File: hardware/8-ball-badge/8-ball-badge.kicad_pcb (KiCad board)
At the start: 2 copper layers, 84 x 84 mm, 88 parts, among them J1 BattConn, J2 SAO Header 1, J3 SAO Header 2, Q1 AO3401A, Q2 S8050, SW1 SW_Push, SW2 TS-1187A-B-A-B, U1 TC4056A, U10 ME6210A33PG, U2 W25Q128JVSIQTR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

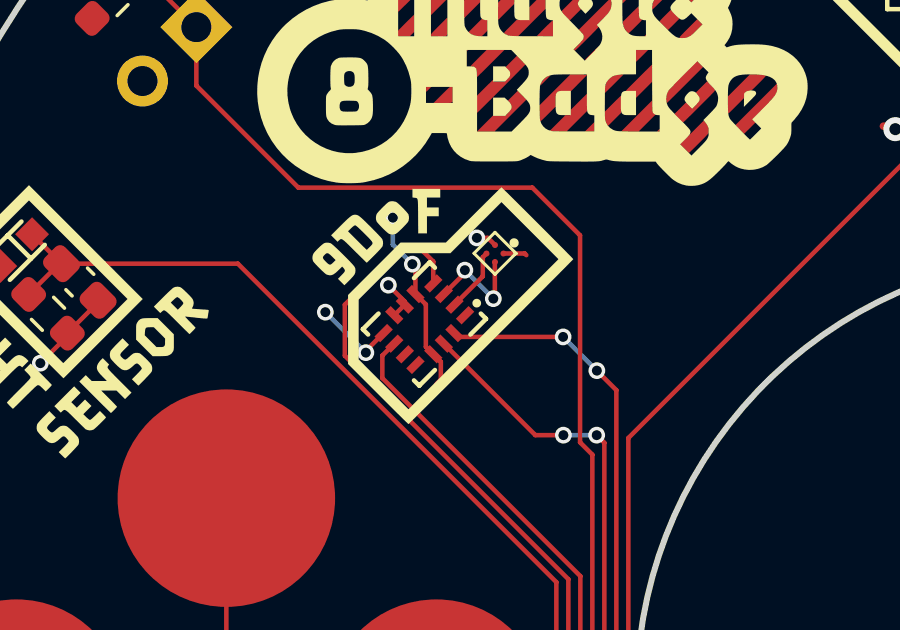
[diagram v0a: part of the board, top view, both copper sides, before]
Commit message: Fix issues with 9DoF chip
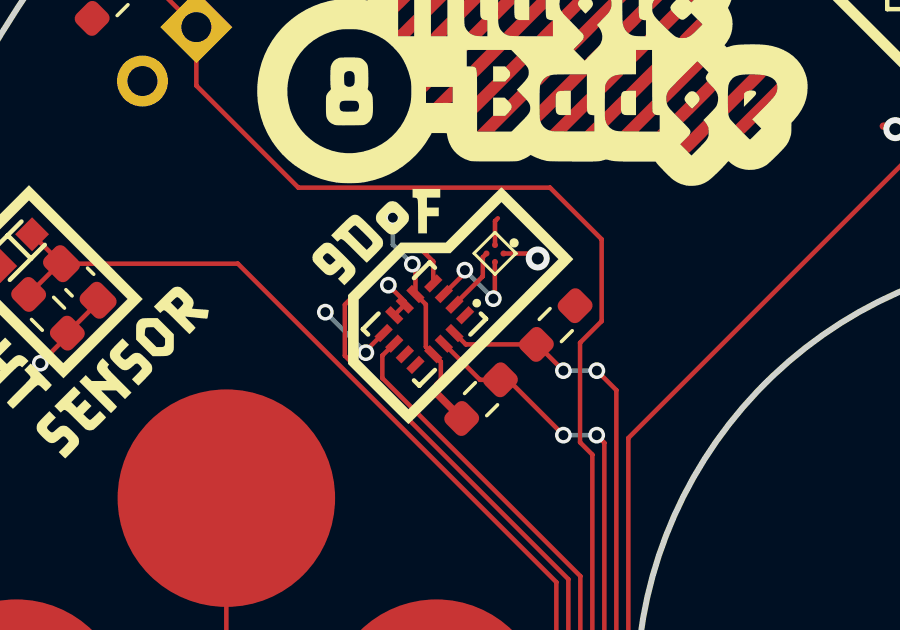
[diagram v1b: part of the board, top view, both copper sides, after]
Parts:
- added R22: 2.4K, Resistor_SMD:R_0603_1608Metric_Pad0.98x0.95mm_HandSolder, F.Cu at (-1.02, 4.23)
- added R23: 2.4K, Resistor_SMD:R_0603_1608Metric_Pad0.98x0.95mm_HandSolder, F.Cu at (-3.51, 6.70)
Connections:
- U9 pad A1: +3V3 -> GND
- U9 pad B1: GND -> +3V3
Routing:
- net +3V3: track 96.8 -> 98.2 mm
- net /SHAKE: track 64.6 -> 65.6 mm
- net GND: track 111.8 -> 112.3 mm
